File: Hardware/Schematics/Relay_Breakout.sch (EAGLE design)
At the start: 15 parts, among them J1 1X2-3.5MM, J2 1X2-3.5MM

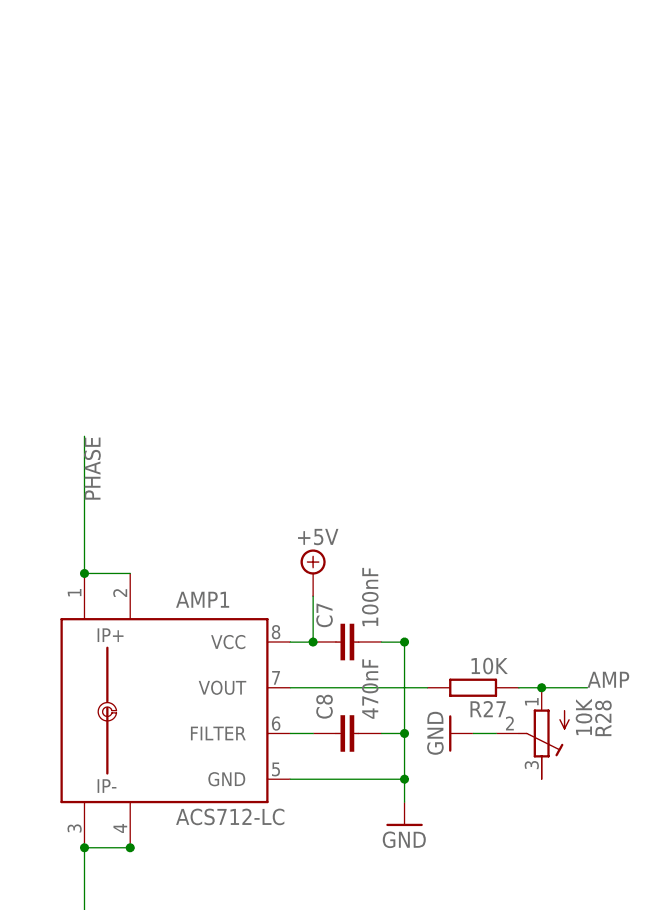
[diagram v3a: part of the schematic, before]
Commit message: Added voltage regulators to both boards. Removed solder mask en 220V traces.
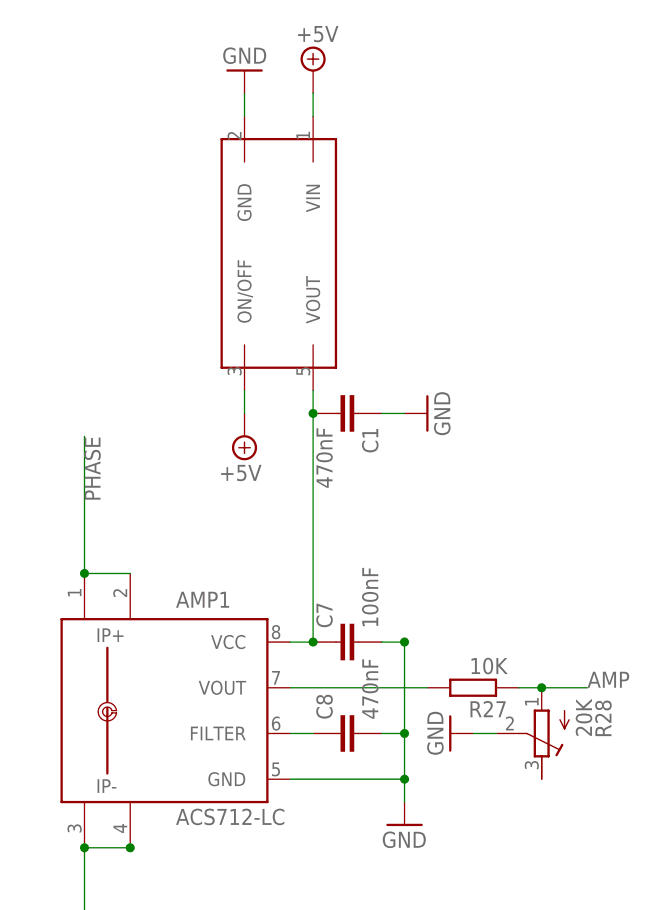
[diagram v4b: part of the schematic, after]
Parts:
- added 4.5V_REG: S1112, PowerSocket:S1112
- added C1: 470nF, rcl:C-EUC0805
- R28: value 10K -> 20K
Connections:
- new net 4.5V: 4.5V_REG.VOUT, AMP1.VCC, C1.2, C7.1
- net +5V: now also 4.5V_REG.ON/OFF, 4.5V_REG.VIN; no longer AMP1.VCC, C7.1
- net GND: now also 4.5V_REG.GND, C1.1
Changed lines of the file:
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@@
 <?xml version="1.0" encoding="utf-8"?>
 <!DOCTYPE eagle SYSTEM "eagle.dtd">
-<eagle version="7.6.0">
+<eagle version="7.7.0">
 <drawing>
 <settings>
@@
 <part name="AMP1" library="allegro-2" deviceset="ACS712-LC" device=""/>
 <part name="GND8" library="supply1" deviceset="GND" device=""/>
-<part name="P+9" library="supply2" deviceset="+5V" device=""/>
 <part name="C7" library="rcl" deviceset="C-EU" device="C0805" value="100nF"/>
 <part name="C8" library="rcl" deviceset="C-EU" device="C0805" value="470nF"/>
 <part name="R27" library="rcl" deviceset="R-EU_" device="R0805" value="10K"/>
-<part name="R28" library="rcl" deviceset="R-TRIMM" device="5X" value="10K"/>
+<part name="R28" library="rcl" deviceset="R-TRIMM" device="5X" value="20K"/>
 <part name="GND12" library="supply1" deviceset="GND" device=""/>
 <part name="U$2" library="SRD-05VDC-SL-C" deviceset="RELAY" device="PTH"/>
@@
 <part name="COPT1" library="supply2" deviceset="+5V" device=""/>
 <part name="GND1" library="supply1" deviceset="GND" device=""/>
+<part name="4.5V_REG" library="PowerSocket" deviceset="S1112" device=""/>
+<part name="COPT2" library="supply2" deviceset="+5V" device=""/>
+<part name="COPT3" library="supply2" deviceset="+5V" device=""/>
+<part name="GND2" library="supply1" deviceset="GND" device=""/>
+<part name="C1" library="rcl" deviceset="C-EU" device="C0805" value="470nF"/>
+<part name="GND3" library="supply1" deviceset="GND" device=""/>
 </parts>
 <sheets>
@@
 <instance part="AMP1" gate="G$1" x="91.44" y="10.16"/>
 <instance part="GND8" gate="1" x="119.38" y="-2.54"/>
-<instance part="P+9" gate="+5V" x="109.22" y="25.4"/>
 <instance part="C7" gate="G$1" x="111.76" y="17.78" rot="R90"/>
 <instance part="C8" gate="G$1" x="111.76" y="7.62" rot="R90"/>
@@
 <instance part="COPT1" gate="+5V" x="50.8" y="-43.18"/>
 <instance part="GND1" gate="1" x="66.04" y="-43.18" rot="R180"/>
+<instance part="4.5V_REG" gate="G$1" x="104.14" y="60.96" rot="R270"/>
+<instance part="COPT2" gate="+5V" x="109.22" y="81.28"/>
+<instance part="COPT3" gate="+5V" x="101.6" y="40.64" rot="R180"/>
+<instance part="GND2" gate="1" x="101.6" y="81.28" rot="R180"/>
+<instance part="C1" gate="G$1" x="114.3" y="43.18" rot="R270"/>
+<instance part="GND3" gate="1" x="121.92" y="43.18" rot="R90"/>
 </instances>
 <busses>
@@
 <pinref part="GND1" gate="1" pin="GND"/>
 </segment>
+<segment>
+<pinref part="4.5V_REG" gate="G$1" pin="GND"/>
+<pinref part="GND2" gate="1" pin="GND"/>
+<wire x1="101.6" y1="76.2" x2="101.6" y2="78.74" width="0.1524" layer="91"/>
+</segment>
+<segment>
+<pinref part="C1" gate="G$1" pin="1"/>
+<pinref part="GND3" gate="1" pin="GND"/>
+<wire x1="116.84" y1="43.18" x2="119.38" y2="43.18" width="0.1524" layer="91"/>
+</segment>
 </net>
 <net name="GATE" class="0">
@@
 </net>
 <net name="+5V" class="0">
-<segment>
-<pinref part="AMP1" gate="G$1" pin="VCC"/>
-<pinref part="C7" gate="G$1" pin="1"/>
-<wire x1="106.68" y1="17.78" x2="109.22" y2="17.78" width="0.1524" layer="91"/>
-<pinref part="P+9" gate="+5V" pin="+5V"/>
-<wire x1="109.22" y1="22.86" x2="109.22" y2="17.78" width="0.1524" layer="91"/>
-<junction x="109.22" y="17.78"/>
-</segment>
 <segment>
 <pinref part="U$3" gate="G$1" pin="COIL1"/>
@@
 <label x="53.34" y="-50.8" size="1.778" layer="95" rot="R90"/>
 <pinref part="COPT1" gate="+5V" pin="+5V"/>
+</segment>
+<segment>
+<pinref part="4.5V_REG" gate="G$1" pin="ON/OFF"/>
+<pinref part="COPT3" gate="+5V" pin="+5V"/>
+<wire x1="101.6" y1="45.72" x2="101.6" y2="43.18" width="0.1524" layer="91"/>
+</segment>
+<segment>
+<pinref part="4.5V_REG" gate="G$1" pin="VIN"/>
+<pinref part="COPT2" gate="+5V" pin="+5V"/>
+<wire x1="109.22" y1="76.2" x2="109.22" y2="78.74" width="0.1524" layer="91"/>
 </segment>
 </net>
@@
 </segment>
 </net>
+<net name="4.5V" class="0">
+<segment>
+<pinref part="4.5V_REG" gate="G$1" pin="VOUT"/>
+<pinref part="C1" gate="G$1" pin="2"/>
+<wire x1="109.22" y1="45.72" x2="109.22" y2="43.18" width="0.1524" layer="91"/>
+<pinref part="AMP1" gate="G$1" pin="VCC"/>
+<pinref part="C7" gate="G$1" pin="1"/>
+<wire x1="106.68" y1="17.78" x2="109.22" y2="17.78" width="0.1524" layer="91"/>
+<wire x1="109.22" y1="43.18" x2="109.22" y2="17.78" width="0.1524" layer="91"/>
+<junction x="109.22" y="17.78"/>
+<junction x="109.22" y="43.18"/>
+</segment>
+</net>
